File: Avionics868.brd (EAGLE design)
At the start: 88.8 x 22.9 mm, 60 parts, among them SW1 SPST_TACT-KMR2, U1 ATSAMD21G18_QFN, U2 SPX3819M5-L-3-0, U3 MCP73831T-2ACI/OT, U4 MPU-9250, U5 SIM868, U6 BMP180, X1 JSTPH, X2 32.768, X3 microUSB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

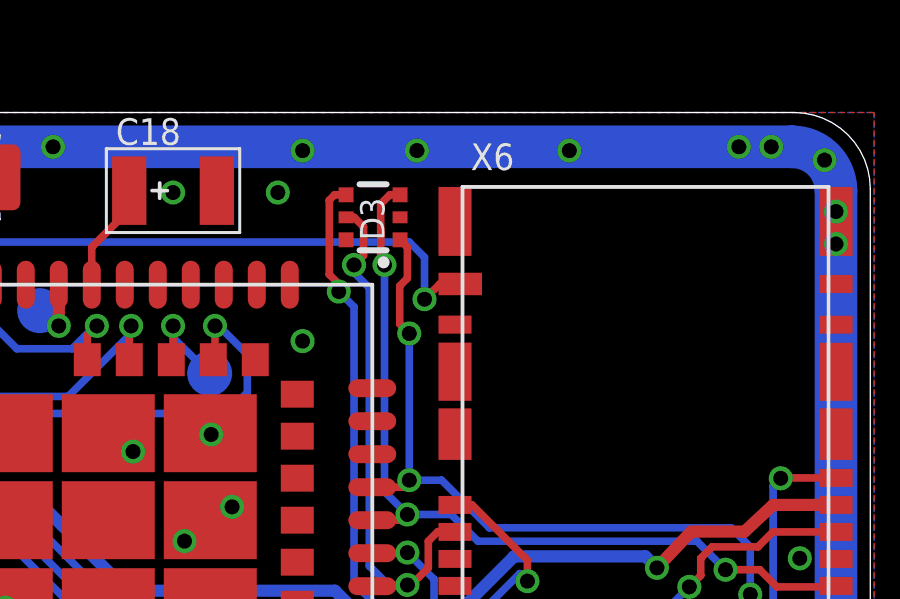
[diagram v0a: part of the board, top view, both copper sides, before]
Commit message: Fixed unconnected microsd chip-select
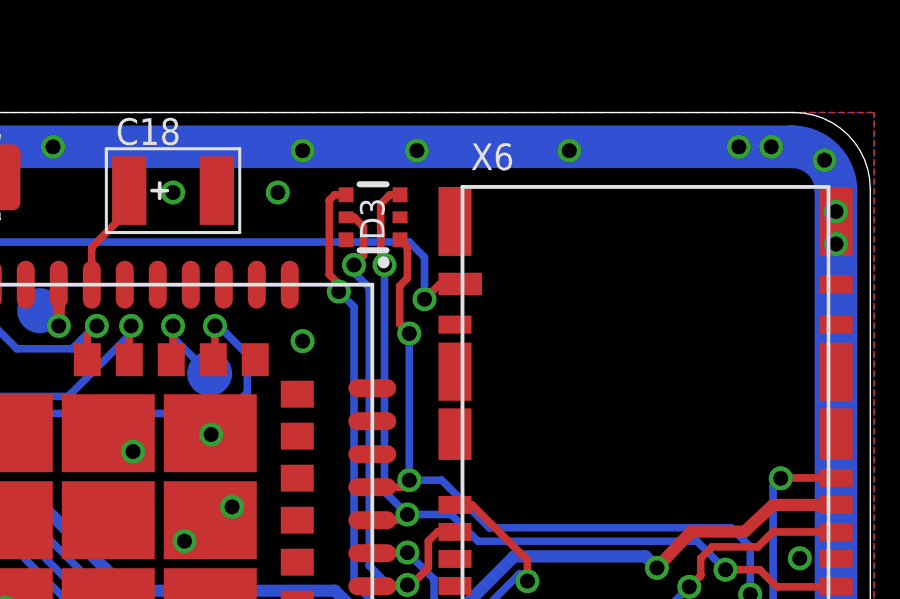
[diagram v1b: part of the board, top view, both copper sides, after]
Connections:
- removed net D4/SD_CS: X6.T2
- removed net D7/SD_DET: U1.30, X6.S/W
- new net D7/SD_CS: U1.30, X6.T2
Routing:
- net D7/SD_DET: track 61.5 -> 0.00 mm, vias 2 -> 0
- net D7/SD_CS: track 0.00 -> 60.8 mm, vias 0 -> 2
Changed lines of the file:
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@@
 <wire x1="63.246" y1="2.667" x2="64.2366" y2="3.429" width="0.254" layer="16"/>
-</signal>
-<signal name="D7/SD_DET">
-<contactref element="U1" pad="30"/>
-<contactref element="X6" pad="S/W"/>
-<wire x1="24.9515" y1="12.6825" x2="24.9515" y2="15.1725" width="0.254" layer="1"/>
-<wire x1="24.9515" y1="15.1725" x2="24.765" y2="15.367" width="0.254" layer="1"/>
-<via x="24.765" y="15.367" extent="1-16" drill="0.5"/>
-<wire x1="24.765" y1="15.367" x2="24.765" y2="13.5255" width="0.254" layer="16"/>
-<wire x1="24.765" y1="13.5255" x2="25.146" y2="13.1445" width="0.254" layer="16"/>
-<wire x1="25.146" y1="13.1445" x2="27.1145" y2="13.1445" width="0.254" layer="16"/>
-<wire x1="27.1145" y1="13.1445" x2="27.813" y2="13.843" width="0.254" layer="16"/>
-<wire x1="75.105" y1="17.145" x2="74.422" y2="17.145" width="0.254" layer="1"/>
-<wire x1="74.422" y1="17.145" x2="73.914" y2="16.637" width="0.254" layer="1"/>
-<via x="73.914" y="16.637" extent="1-16" drill="0.5"/>
-<wire x1="73.914" y1="16.637" x2="73.914" y2="18.034" width="0.254" layer="16"/>
-<wire x1="27.813" y1="13.843" x2="28.5115" y2="13.843" width="0.254" layer="16"/>
-<wire x1="28.5115" y1="13.843" x2="28.8925" y2="13.462" width="0.254" layer="16"/>
-<wire x1="28.8925" y1="13.462" x2="31.6865" y2="13.462" width="0.254" layer="16"/>
-<wire x1="31.6865" y1="13.462" x2="33.401" y2="15.1765" width="0.254" layer="16"/>
-<wire x1="33.401" y1="15.1765" x2="37.084" y2="15.1765" width="0.254" layer="16"/>
-<wire x1="44.323" y1="15.748" x2="42.9895" y2="15.748" width="0.254" layer="16"/>
-<wire x1="44.323" y1="15.748" x2="44.577" y2="15.494" width="0.254" layer="16"/>
-<wire x1="44.577" y1="15.494" x2="44.577" y2="15.0495" width="0.254" layer="16"/>
-<wire x1="44.577" y1="15.0495" x2="44.958" y2="14.6685" width="0.254" layer="16"/>
-<wire x1="37.084" y1="15.1765" x2="38.6715" y2="16.764" width="0.254" layer="16"/>
-<wire x1="38.6715" y1="16.764" x2="41.9735" y2="16.764" width="0.254" layer="16"/>
-<wire x1="41.9735" y1="16.764" x2="42.9895" y2="15.748" width="0.254" layer="16"/>
-<wire x1="44.958" y1="14.6685" x2="46.9265" y2="14.6685" width="0.254" layer="16"/>
-<wire x1="46.9265" y1="14.6685" x2="50.8" y2="18.542" width="0.254" layer="16"/>
-<wire x1="50.8" y1="18.542" x2="73.406" y2="18.542" width="0.254" layer="16"/>
-<wire x1="73.406" y1="18.542" x2="73.914" y2="18.034" width="0.254" layer="16"/>
 </signal>
 <signal name="GPS_EN">
@@
 <wire x1="67.056" y1="15.748" x2="66.929" y2="15.748" width="0.254" layer="16"/>
 </signal>
-<signal name="D4/SD_CS">
+<signal name="D7/SD_CS">
 <contactref element="X6" pad="T2"/>
+<contactref element="U1" pad="30"/>
+<wire x1="24.9515" y1="12.6825" x2="24.9515" y2="15.1725" width="0.254" layer="1"/>
+<wire x1="24.9515" y1="15.1725" x2="24.765" y2="15.367" width="0.254" layer="1"/>
+<via x="24.765" y="15.367" extent="1-16" drill="0.5"/>
+<wire x1="24.765" y1="15.367" x2="24.765" y2="13.5255" width="0.254" layer="16"/>
+<wire x1="24.765" y1="13.5255" x2="25.146" y2="13.1445" width="0.254" layer="16"/>
+<wire x1="25.146" y1="13.1445" x2="27.1145" y2="13.1445" width="0.254" layer="16"/>
+<wire x1="27.1145" y1="13.1445" x2="27.813" y2="13.843" width="0.254" layer="16"/>
+<wire x1="74.422" y1="17.145" x2="73.914" y2="16.637" width="0.254" layer="1"/>
+<via x="73.914" y="16.637" extent="1-16" drill="0.5"/>
+<wire x1="73.914" y1="16.637" x2="73.914" y2="18.034" width="0.254" layer="16"/>
+<wire x1="27.813" y1="13.843" x2="28.5115" y2="13.843" width="0.254" layer="16"/>
+<wire x1="28.5115" y1="13.843" x2="28.8925" y2="13.462" width="0.254" layer="16"/>
+<wire x1="28.8925" y1="13.462" x2="31.6865" y2="13.462" width="0.254" layer="16"/>
+<wire x1="31.6865" y1="13.462" x2="33.401" y2="15.1765" width="0.254" layer="16"/>
+<wire x1="33.401" y1="15.1765" x2="37.084" y2="15.1765" width="0.254" layer="16"/>
+<wire x1="44.323" y1="15.748" x2="42.9895" y2="15.748" width="0.254" layer="16"/>
+<wire x1="44.323" y1="15.748" x2="44.577" y2="15.494" width="0.254" layer="16"/>
+<wire x1="44.577" y1="15.494" x2="44.577" y2="15.0495" width="0.254" layer="16"/>
+<wire x1="44.577" y1="15.0495" x2="44.958" y2="14.6685" width="0.254" layer="16"/>
+<wire x1="37.084" y1="15.1765" x2="38.6715" y2="16.764" width="0.254" layer="16"/>
+<wire x1="38.6715" y1="16.764" x2="41.9735" y2="16.764" width="0.254" layer="16"/>
+<wire x1="41.9735" y1="16.764" x2="42.9895" y2="15.748" width="0.254" layer="16"/>
+<wire x1="44.958" y1="14.6685" x2="46.9265" y2="14.6685" width="0.254" layer="16"/>
+<wire x1="46.9265" y1="14.6685" x2="50.8" y2="18.542" width="0.254" layer="16"/>
+<wire x1="50.8" y1="18.542" x2="73.406" y2="18.542" width="0.254" layer="16"/>
+<wire x1="73.406" y1="18.542" x2="73.914" y2="18.034" width="0.254" layer="16"/>
+<wire x1="74.422" y1="17.145" x2="87.63" y2="15.79" width="0" layer="19" extent="1-1"/>
 </signal>
 <signal name="MPU_INT">

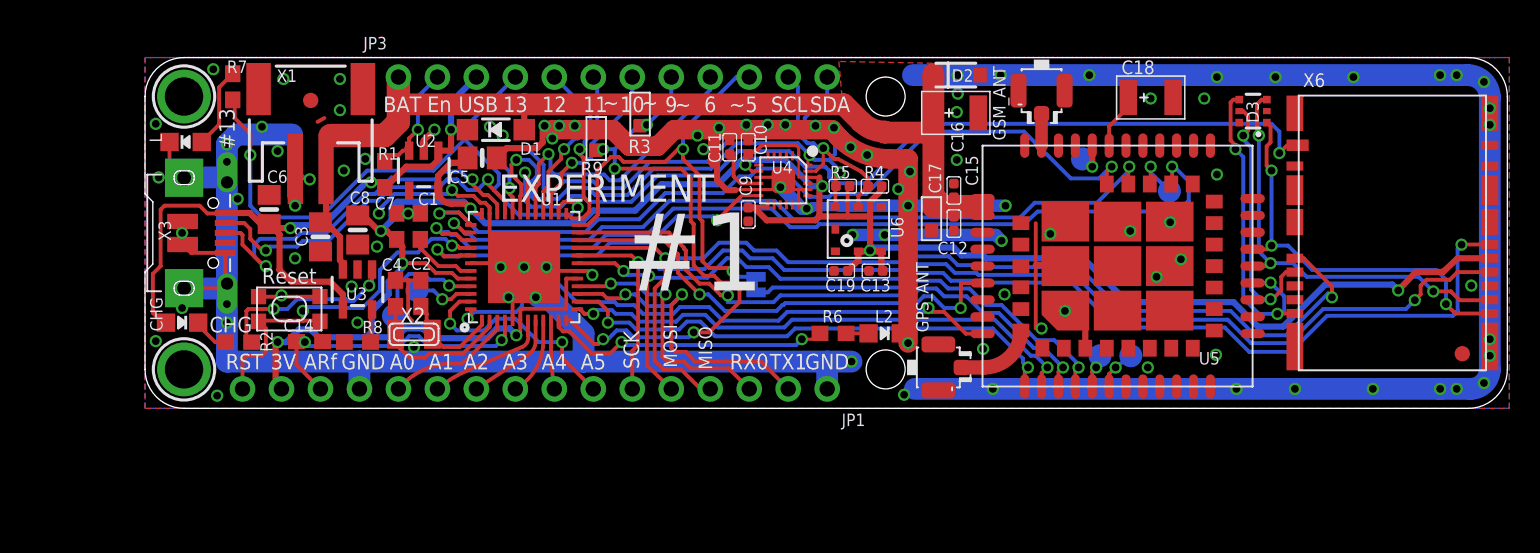
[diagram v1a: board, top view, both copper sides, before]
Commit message: Prev. commit was faulty, only half fixed Also fixed a number of ERC/DRC issues
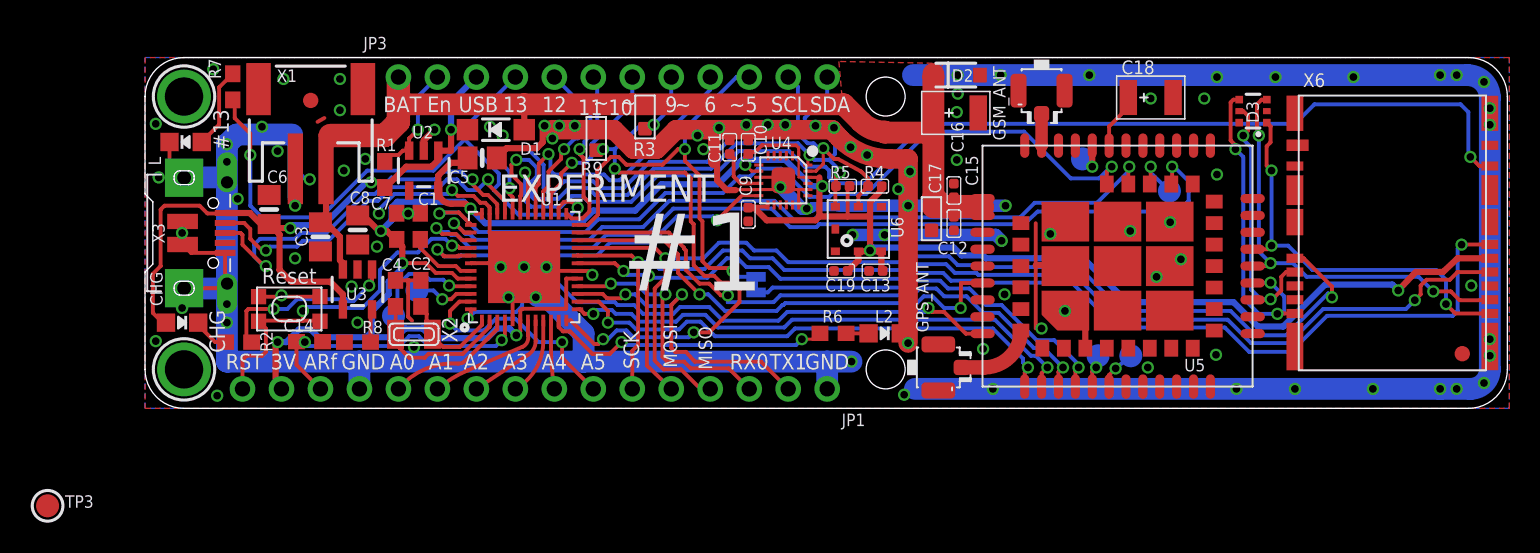
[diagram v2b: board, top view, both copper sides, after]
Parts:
- added TP3: (no value), microbuilder:TESTPOINT_ROUND_1.5MM
- moved R3 0.37 mm to (32.6, 19.0)
- moved TP6 0.13 mm to (62.1, 3.43)
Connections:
- new net SD_DET: TP3.P$1, X6.S/W
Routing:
- net D7/SD_CS: track 60.8 -> 76.0 mm

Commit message: Placed pad for SD_DET
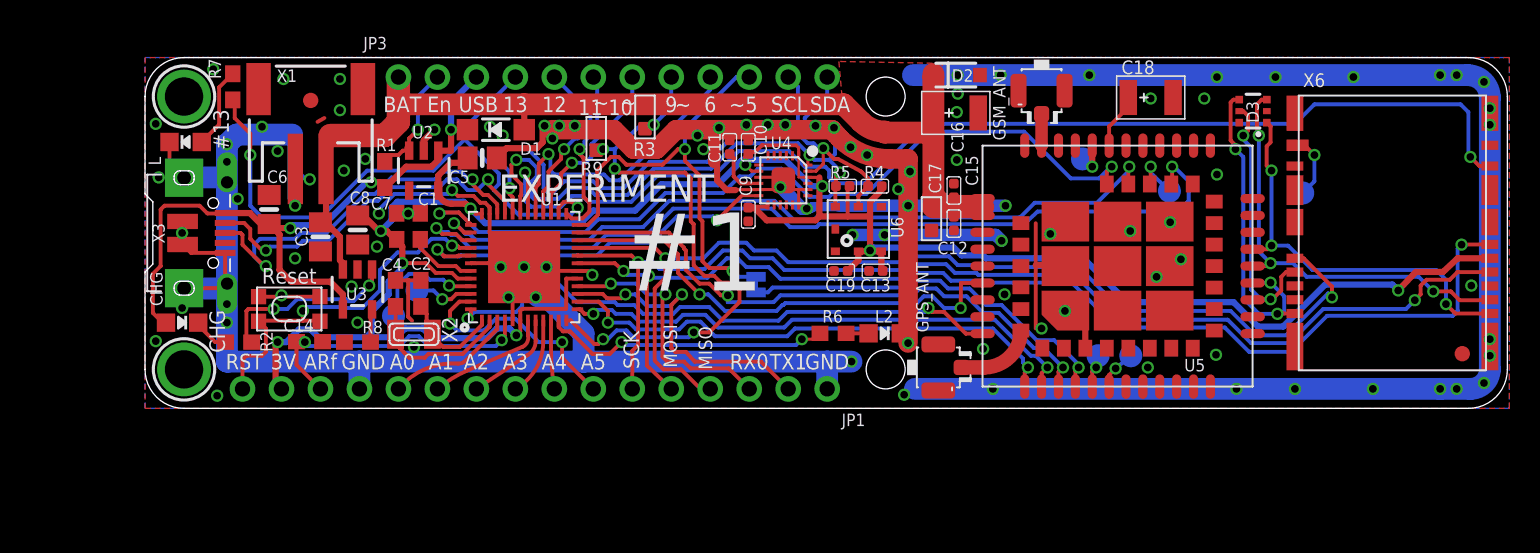
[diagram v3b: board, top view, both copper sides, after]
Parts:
- moved TP3 84.3 mm to (75.4, 14.0), flipped to the bottom
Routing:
- net SD_DET: track 0.00 -> 4.15 mm, vias 0 -> 1
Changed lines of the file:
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@@
 <attribute name="VALUE" x="27.9655" y="19.1945" size="0.635" layer="27" ratio="10" rot="R270"/>
 </element>
-<element name="TP3" library="microbuilder" package="TESTPOINT_ROUND_1.5MM" value="" x="-6.35" y="-6.35"/>
+<element name="TP3" library="microbuilder" package="TESTPOINT_ROUND_1.5MM" value="" x="75.438" y="14.0335" rot="MR0"/>
 </elements>
 <signals>
@@
 <contactref element="X6" pad="S/W"/>
 <contactref element="TP3" pad="P$1"/>
-<wire x1="-6.35" y1="-6.35" x2="75.105" y2="17.145" width="0" layer="19" extent="1-1"/>
+<wire x1="75.105" y1="17.145" x2="75.565" y2="17.145" width="0.254" layer="1"/>
+<wire x1="75.565" y1="17.145" x2="76.2" y2="16.51" width="0.254" layer="1"/>
+<via x="76.2" y="16.51" extent="1-16" drill="0.5"/>
+<wire x1="76.2" y1="16.51" x2="76.2" y2="14.7955" width="0.254" layer="16"/>
+<wire x1="76.2" y1="14.7955" x2="75.438" y2="14.0335" width="0.254" layer="16"/>
 </signal>
 </signals>

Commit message: Added libraries
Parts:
- L3: value ORANGE -> BLUE
- renumbered CHG to L3, L to L1
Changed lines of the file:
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@@
 <setting verticaltext="up"/>
 </settings>
-<grid distance="0.05" unitdist="inch" unit="inch" style="lines" multiple="1" display="no" altdistance="0.0025" altunitdist="inch" altunit="inch"/>
+<grid distance="0.05" unitdist="inch" unit="mm" style="lines" multiple="1" display="no" altdistance="0.0025" altunitdist="inch" altunit="inch"/>
 <layers>
 <layer number="1" name="Top" color="4" fill="1" visible="yes" active="yes"/>
@@
 <text x="45.974" y="21.463" size="1.016" layer="22" font="vector" ratio="12" rot="SMR270" align="center">20</text>
 <text x="43.18" y="21.463" size="0.889" layer="22" font="vector" ratio="12" rot="SMR270" align="center">21</text>
-<dimension x1="0" y1="18.796" x2="88.773" y2="19.558" x3="44.3865" y3="45.974" textsize="1.778" layer="47" dtype="horizontal" unit="inch"/>
+<dimension x1="0" y1="18.796" x2="88.773" y2="19.558" x3="44.3865" y3="45.974" textsize="1.778" layer="47" dtype="horizontal"/>
 <dimension x1="2.54" y1="20.32" x2="48.26" y2="20.32" x3="25.4" y3="32.258" textsize="1.778" layer="47" dtype="horizontal" unit="inch"/>
 <dimension x1="0" y1="20.955" x2="10.795" y2="19.304" x3="5.3975" y3="24.384" textsize="1.778" layer="47" dtype="horizontal" unit="inch"/>
@@
 <dimension x1="88.9" y1="21.59" x2="89.027" y2="19.05" x3="95.504" y3="20.32" textsize="1.778" layer="47" dtype="vertical" unit="inch"/>
 <dimension x1="1.397" y1="2.413" x2="3.81" y2="2.413" x3="2.6035" y3="-2.921" textsize="1.778" layer="47" unit="inch"/>
-<dimension x1="3.683" y1="0" x2="5.207" y2="22.86" x3="-5.588" y3="11.43" textsize="1.778" layer="47" dtype="vertical" unit="inch"/>
+<dimension x1="3.683" y1="0" x2="5.207" y2="22.86" x3="-5.588" y3="11.43" textsize="1.778" layer="47" dtype="vertical"/>
 <dimension x1="3.556" y1="0" x2="4.445" y2="11.43" x3="-2.032" y3="5.715" textsize="1.778" layer="47" dtype="vertical" unit="inch"/>
 <dimension x1="88.9" y1="21.59" x2="88.9" y2="1.27" x3="100.965" y3="11.43" textsize="1.778" layer="47" dtype="vertical" unit="inch"/>
@@
 <attribute name="VALUE" x="13.48" y="12.9194" size="0.8128" layer="27" ratio="10" rot="R270"/>
 </element>
-<element name="L" library="microbuilder" package="CHIPLED_0805_NOOUTLINE" value="RED" x="2.645" y="17.359" smashed="yes" rot="R90">
+<element name="L1" library="microbuilder" package="CHIPLED_0805_NOOUTLINE" value="RED" x="2.645" y="17.359" smashed="yes" rot="R90">
 <attribute name="NAME" x="1.0395" y="15.8335" size="0.8128" layer="25" ratio="18" rot="R90"/>
 <attribute name="VALUE" x="-0.657" y="17.74" size="0.8128" layer="27" ratio="10" rot="R180"/>
@@
 <attribute name="VALUE" x="19.993" y="-1.016" size="0.8128" layer="27" ratio="10" rot="R180"/>
 </element>
-<element name="CHG" library="microbuilder" package="CHIPLED_0805_NOOUTLINE" value="ORANGE" x="2.413" y="5.588" smashed="yes" rot="R270">
+<element name="L3" library="microbuilder" package="CHIPLED_0805_NOOUTLINE" value="BLUE" x="2.413" y="5.588" smashed="yes" rot="R270">
 <attribute name="NAME" x="1.143" y="6.6675" size="0.8128" layer="25" ratio="18" rot="R90"/>
 <attribute name="VALUE" x="0" y="5.842" size="0.8128" layer="27" ratio="10" rot="R180"/>
@@
 <contactref element="X3" pad="BASE@1"/>
 <contactref element="U2" pad="2"/>
-<contactref element="L" pad="C"/>
+<contactref element="L1" pad="C"/>
 <contactref element="JP1" pad="13"/>
 <contactref element="X1" pad="1"/>
@@
 <contactref element="JP3" pad="3"/>
 <contactref element="U3" pad="4"/>
-<contactref element="CHG" pad="A"/>
+<contactref element="L3" pad="A"/>
 <wire x1="5.22" y1="12.73" x2="6.828" y2="12.73" width="0.4064" layer="1"/>
 <wire x1="1.363" y1="5.588" x2="1.143" y2="5.588" width="0.254" layer="1"/>
@@
 </signal>
 <signal name="N$2">
-<contactref element="L" pad="A"/>
+<contactref element="L1" pad="A"/>
 <contactref element="R7" pad="2"/>
 <wire x1="3.695" y1="17.359" x2="4.826" y2="18.49" width="0.254" layer="1"/>
@@
 </signal>
 <signal name="N$1">
-<contactref element="CHG" pad="C"/>
+<contactref element="L3" pad="C"/>
 <contactref element="R2" pad="1"/>
 <wire x1="3.463" y1="5.588" x2="3.463" y2="5.427" width="0.254" layer="1"/>
